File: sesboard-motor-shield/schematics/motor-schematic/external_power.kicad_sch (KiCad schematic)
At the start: 21 parts, among them Q1 Q_NMOS_DGS, Q2 TIP3055, U1 LM317_SOT-223, U4 AMS1117-5.0

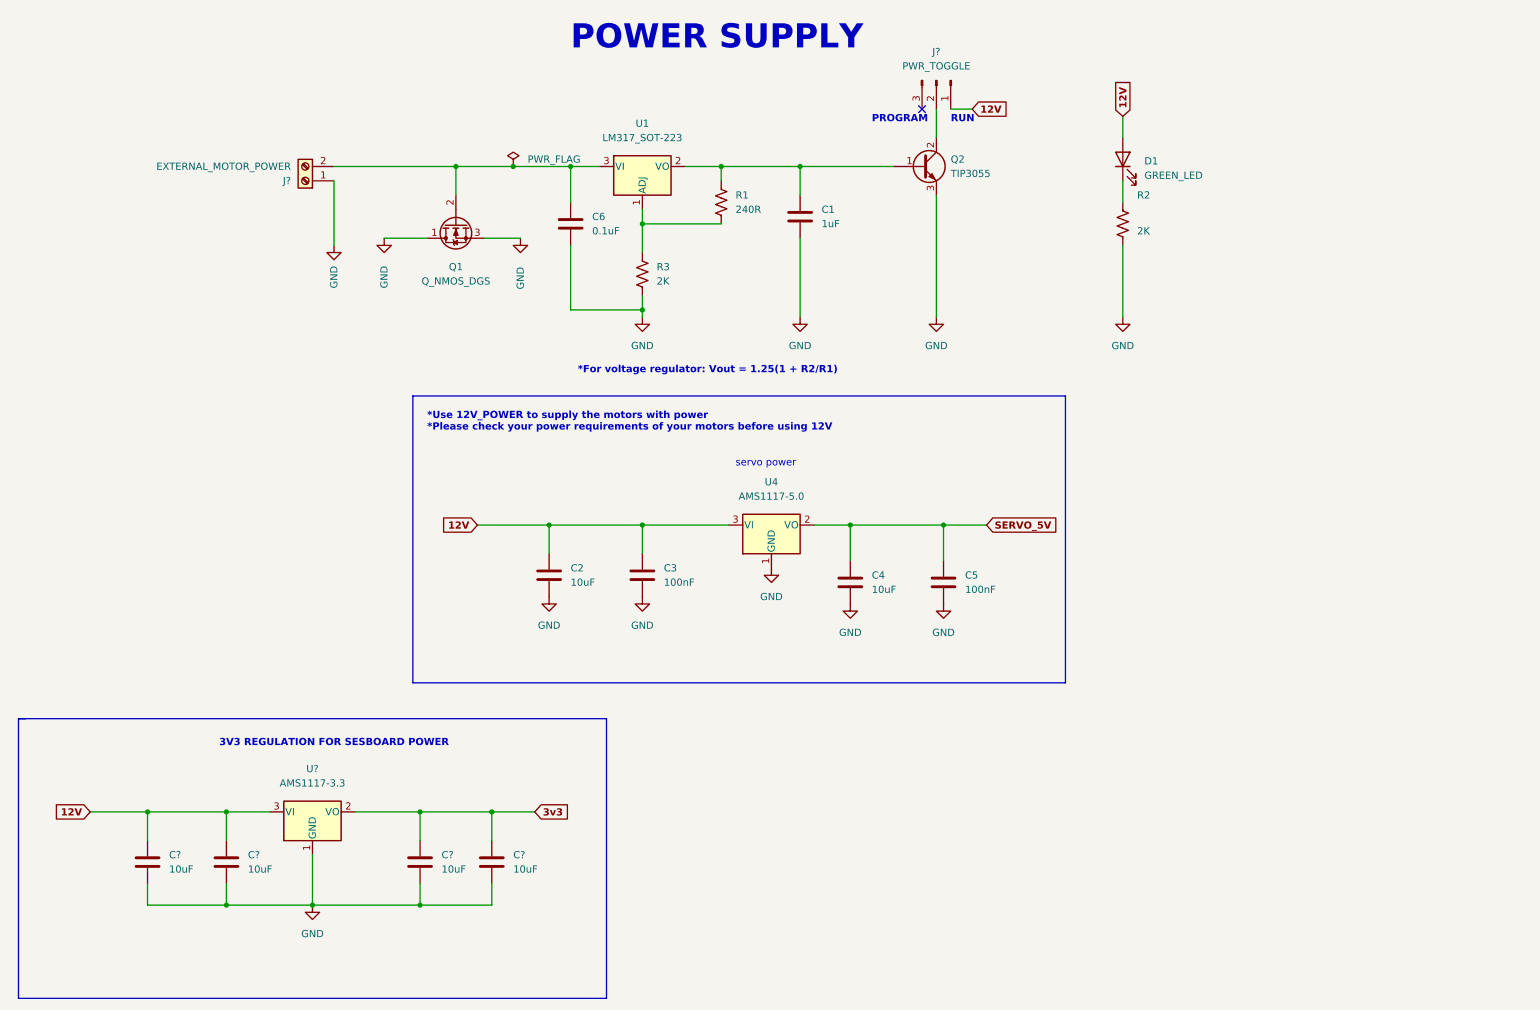
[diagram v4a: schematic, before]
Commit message: added stepper connector
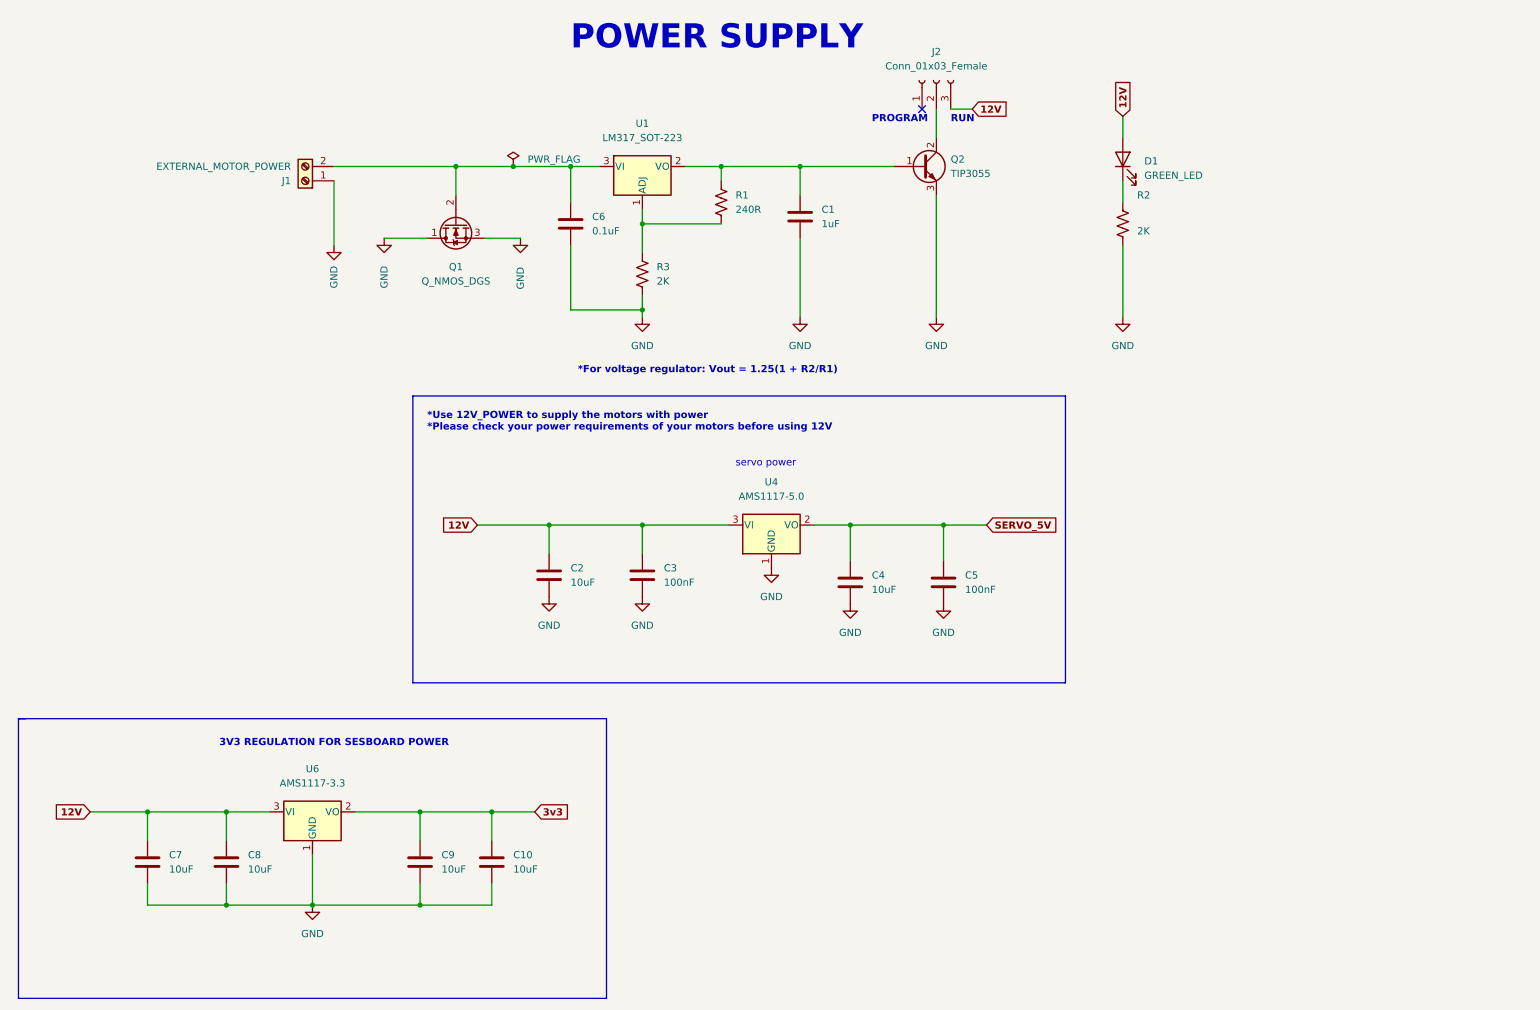
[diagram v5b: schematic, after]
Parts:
- removed J?: PWR_TOGGLE, symbol Connector:Conn_01x03_Male
- added J2: Conn_01x03_Female, Connector_PinHeader_2.54mm:PinHeader_1x03_P2.54mm_Vertical, symbol Connector:Conn_01x03_Female
- gave numbers to parts that had none: 6
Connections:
- net 12V: now also J2.3 (Pin_3)
- net at Q2.2 (C): now also J2.2 (Pin_2)
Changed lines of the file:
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@@
   (symbol (lib_id "power:GND") (at 73.66 172.72 0) (unit 1)
     (in_bom yes) (on_board yes) (fields_autoplaced)
-    (property "Reference" "#PWR?" (id 0) (at 73.66 179.07 0)
+    (property "Reference" "#PWR05" (id 0) (at 73.66 179.07 0)
       (effects (font (size 1.27 1.27)) hide)
     )
@@
   (symbol (lib_id "Device:C") (at 105.41 165.1 0) (unit 1)
     (in_bom yes) (on_board yes) (fields_autoplaced)
-    (property "Reference" "C?" (id 0) (at 109.22 163.8299 0)
+    (property "Reference" "C10" (id 0) (at 109.22 163.8299 0)
       (effects (font (size 1.27 1.27)) (justify left))
     )
@@
     (pin "1")
     (pin "2")
+  )
+  (symbol (lib_id "Connector:Conn_01x03_Female") (at 184.15 26.67 90) (unit 1)
+    (in_bom yes) (on_board yes) (fields_autoplaced)
+    (property "Reference" "J2" (id 0) (at 184.15 21.59 90))
+    (property "Value" "Conn_01x03_Female" (id 1) (at 184.15 24.13 90))
+    (property "Footprint" "Connector_PinHeader_2.54mm:PinHeader_1x03_P2.54mm_Vertical" (id 2) (at 184.15 26.67 0)
+      (effects (font (size 1.27 1.27)) hide)
+    )
+    (property "Datasheet" "~" (id 3) (at 184.15 26.67 0)
+      (effects (font (size 1.27 1.27)) hide)
+    )
+    (pin "1")
+    (pin "2")
+    (pin "3")
   )
   (symbol (lib_id "power:GND") (at 185.42 119.38 0) (unit 1)
@@
     (pin "1")
   )
-  (symbol (lib_id "Connector:Conn_01x03_Male") (at 184.15 26.67 270) (unit 1)
-    (in_bom yes) (on_board yes) (fields_autoplaced)
-    (property "Reference" "J?" (id 0) (at 184.15 21.59 90))
-    (property "Value" "PWR_TOGGLE" (id 1) (at 184.15 24.13 90))
-    (property "Footprint" "" (id 2) (at 184.15 26.67 0)
-      (effects (font (size 1.27 1.27)) hide)
-    )
-    (property "Datasheet" "~" (id 3) (at 184.15 26.67 0)
-      (effects (font (size 1.27 1.27)) hide)
-    )
-    (pin "1")
-    (pin "2")
-    (pin "3")
-  )
   (symbol (lib_id "power:GND") (at 154.94 113.03 0) (unit 1)
     (in_bom yes) (on_board yes) (fields_autoplaced)
@@
   (symbol (lib_id "Device:C") (at 44.45 165.1 0) (unit 1)
     (in_bom yes) (on_board yes) (fields_autoplaced)
-    (property "Reference" "C?" (id 0) (at 48.26 163.8299 0)
+    (property "Reference" "C7" (id 0) (at 48.26 163.8299 0)
       (effects (font (size 1.27 1.27)) (justify left))
     )
@@
   (symbol (lib_id "Connector:Screw_Terminal_01x02") (at 72.39 44.45 180) (unit 1)
     (in_bom yes) (on_board yes) (fields_autoplaced)
-    (property "Reference" "J?" (id 0) (at 69.85 44.4501 0)
+    (property "Reference" "J1" (id 0) (at 69.85 44.4501 0)
       (effects (font (size 1.27 1.27)) (justify left))
     )
@@
   (symbol (lib_id "Device:C") (at 58.42 165.1 0) (unit 1)
     (in_bom yes) (on_board yes) (fields_autoplaced)
-    (property "Reference" "C?" (id 0) (at 62.23 163.8299 0)
+    (property "Reference" "C8" (id 0) (at 62.23 163.8299 0)
       (effects (font (size 1.27 1.27)) (justify left))
     )
@@
   (symbol (lib_id "Device:C") (at 92.71 165.1 0) (unit 1)
     (in_bom yes) (on_board yes) (fields_autoplaced)
-    (property "Reference" "C?" (id 0) (at 96.52 163.8299 0)
+    (property "Reference" "C9" (id 0) (at 96.52 163.8299 0)
       (effects (font (size 1.27 1.27)) (justify left))
     )
@@
   (symbol (lib_id "Regulator_Linear:AMS1117-3.3") (at 73.66 156.21 0) (unit 1)
     (in_bom yes) (on_board yes) (fields_autoplaced)
-    (property "Reference" "U?" (id 0) (at 73.66 148.59 0))
+    (property "Reference" "U6" (id 0) (at 73.66 148.59 0))
     (property "Value" "AMS1117-3.3" (id 1) (at 73.66 151.13 0))
     (property "Footprint" "Package_TO_SOT_SMD:SOT-223-3_TabPin2" (id 2) (at 73.66 151.13 0)

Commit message: added view image
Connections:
- net 12V: no longer C7.1, C8.1, U6.3 (VI)
- net SERVO_5V: now also C7.1, C8.1, U6.3 (VI)
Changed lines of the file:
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@@
     )
   )
-  (global_label "12V" (shape input) (at 34.29 156.21 180) (fields_autoplaced)
+  (global_label "SERVO_5V" (shape input) (at 34.29 156.21 180) (fields_autoplaced)
     (effects (font (size 1.27 1.27) bold) (justify right))
-    (property "Intersheet References" "${INTERSHEET_REFS}" (id 0) (at 28.1789 156.083 0)
+    (property "Intersheet References" "${INTERSHEET_REFS}" (id 0) (at 22.3732 156.337 0)
       (effects (font (size 1.27 1.27) bold) (justify right) hide)
     )
